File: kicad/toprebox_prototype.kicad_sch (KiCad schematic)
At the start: 1 part, among them U1 YAAJ_BlackPill_Part_Like

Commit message: completed matrix
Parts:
- U1: footprint (none) -> footprints:YAAJ_BlackPill_1
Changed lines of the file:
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@@
 			)
 		)
-		(property "Footprint" ""
+		(property "Footprint" "footprints:YAAJ_BlackPill_1"
 			(at 106.68 43.18 0)
 			(effects

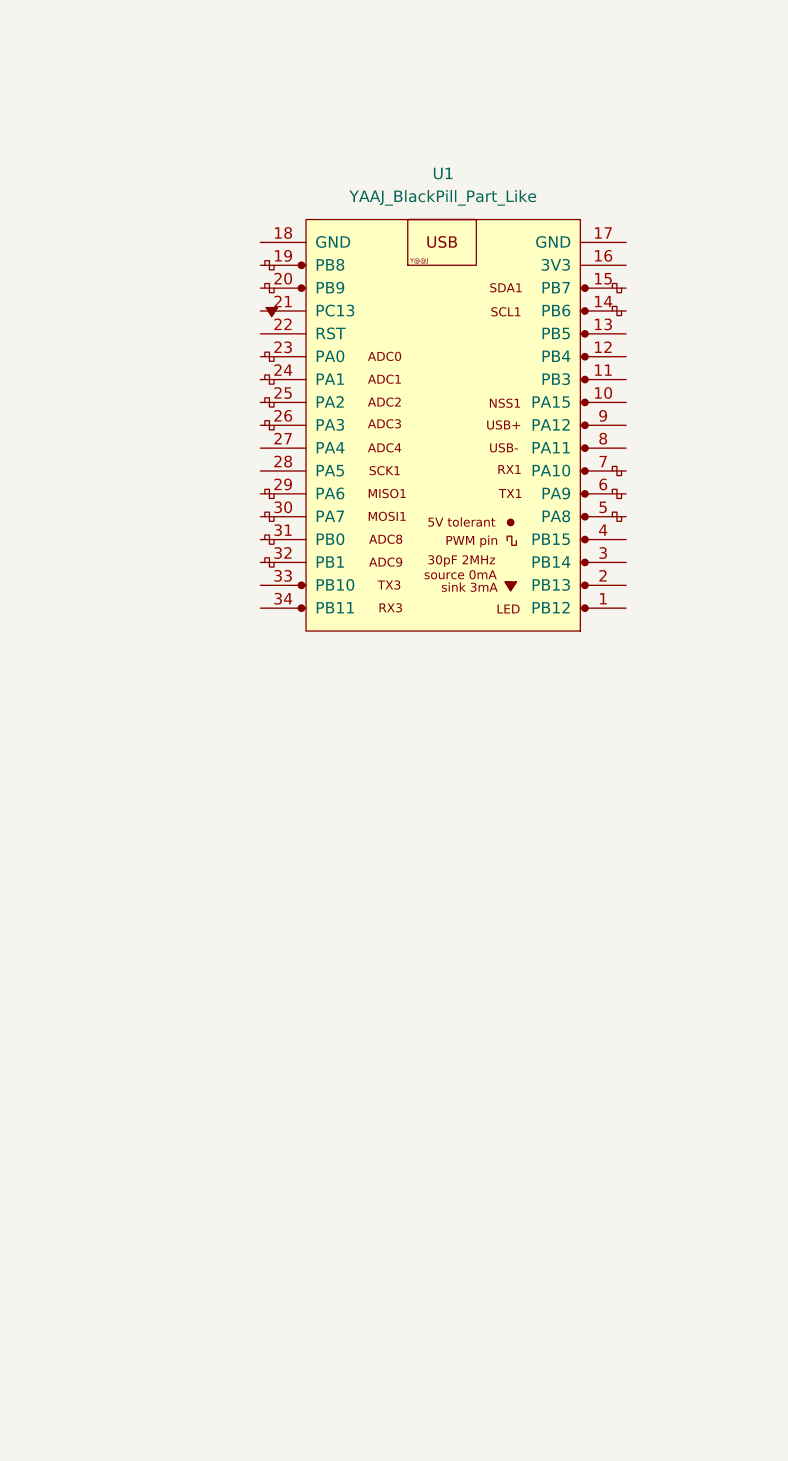
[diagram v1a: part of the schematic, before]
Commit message: replaced half of the matrix
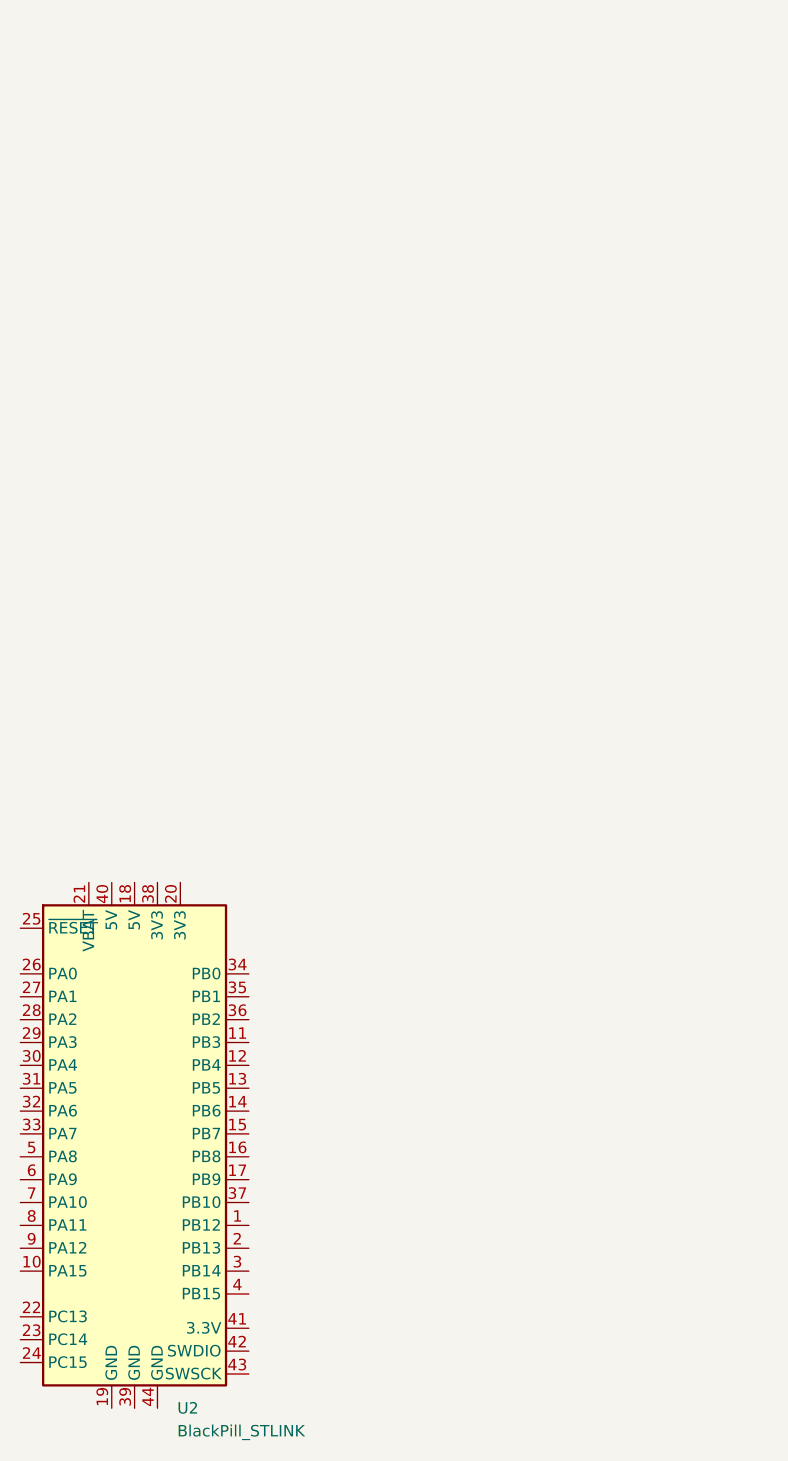
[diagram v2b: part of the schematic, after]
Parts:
- removed U1: YAAJ_BlackPill_Part_Like, footprints:YAAJ_BlackPill_1, symbol YAAJ_BlackPill_Part_Like:YAAJ_BlackPill_Part_Like
- added U2: BlackPill_STLINK, footprints:WeAct_BlackPill_without_SWD_First_Row, symbol blackpill_stlink:BlackPill_STLINK
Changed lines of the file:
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@@
 	(paper "A4")
 	(symbol
-		(lib_id "YAAJ_BlackPill_Part_Like:YAAJ_BlackPill_Part_Like")
-		(at 123.19 73.66 180)
+		(lib_id "blackpill_stlink:BlackPill_STLINK")
+		(at 88.9 154.94 0)
 		(unit 1)
 		(exclude_from_sim no)
@@
 		(dnp no)
 		(fields_autoplaced yes)
-		(property "Reference" "U1"
-			(at 123.19 45.72 0)
+		(property "Reference" "U2"
+			(at 93.6341 182.88 0)
 			(effects
 				(font
 					(size 1.27 1.27)
 				)
+				(justify left)
 			)
 		)
-		(property "Value" "YAAJ_BlackPill_Part_Like"
-			(at 123.19 48.26 0)
+		(property "Value" "BlackPill_STLINK"
+			(at 93.6341 185.42 0)
 			(effects
 				(font
 					(size 1.27 1.27)
 				)
+				(justify left)
 			)
 		)
-		(property "Footprint" "footprints:YAAJ_BlackPill_1"
-			(at 106.68 43.18 0)
+		(property "Footprint" "footprints:WeAct_BlackPill_without_SWD_First_Row"
+			(at 132.08 156.21 0)
 			(effects
 				(font
@@
 		)
 		(property "Datasheet" ""
-			(at 106.68 43.18 0)
+			(at 132.08 156.21 0)
 			(effects
 				(font
@@
 			)
 		)
-		(property "Description" ""
-			(at 123.19 73.66 0)
+		(property "Description" "STM32F4-based \"Black Pill\" micro-controller development board"
+			(at 88.9 154.94 0)
 			(effects
 				(font
@@
 			)
 		)
+		(pin "38"
+		)
+		(pin "30"
+		)
+		(pin "16"
+		)
+		(pin "4"
+		)
+		(pin "34"
+		)
+		(pin "6"
+		)
+		(pin "5"
+		)
+		(pin "7"
+		)
+		(pin "10"
+		)
+		(pin "22"
+		)
+		(pin "8"
+		)
+		(pin "26"
+		)
+		(pin "31"
+		)
+		(pin "21"
+		)
+		(pin "43"
+		)
+		(pin "36"
+		)
+		(pin "18"
+		)
+		(pin "37"
+		)
+		(pin "41"
+		)
 		(pin "28"
-		)
-		(pin "19"
 		)
 		(pin "9"
 		)
-		(pin "7"
+		(pin "17"
 		)
-		(pin "6"
+		(pin "40"
 		)
-		(pin "8"
-		)
-		(pin "16"
-		)
-		(pin "10"
-		)
-		(pin "11"
-		)
-		(pin "22"
-		)
-		(pin "15"
-		)
-		(pin "21"
-		)
-		(pin "31"
-		)
-		(pin "14"
-		)
-		(pin "13"
-		)
-		(pin "12"
-		)
-		(pin "1"
+		(pin "27"
 		)
 		(pin "20"
@@
 		(pin "25"
 		)
-		(pin "18"
+		(pin "23"
+		)
+		(pin "32"
+		)
+		(pin "33"
+		)
+		(pin "44"
+		)
+		(pin "35"
+		)
+		(pin "2"
+		)
+		(pin "39"
 		)
 		(pin "24"
 		)
-		(pin "32"
-		)
-		(pin "4"
-		)
-		(pin "27"
+		(pin "42"
 		)
 		(pin "29"
 		)
-		(pin "2"
+		(pin "1"
 		)
-		(pin "33"
+		(pin "13"
 		)
-		(pin "5"
+		(pin "19"
 		)
-		(pin "23"
+		(pin "11"
 		)
-		(pin "26"
+		(pin "12"
 		)
-		(pin "30"
+		(pin "14"
 		)
-		(pin "17"
-		)
-		(pin "34"
+		(pin "15"
 		)
 		(pin "3"
@@
 			(project ""
 				(path "/8da5c518-ba63-450e-856e-258a7a1195e6"
-					(reference "U1")
+					(reference "U2")
 					(unit 1)
 				)

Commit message: stuff
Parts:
- removed U2: BlackPill_STLINK, footprints:WeAct_BlackPill_without_SWD_First_Row, symbol blackpill_stlink:BlackPill_STLINK
- added C5, C7, C8: 100n, Capacitor_SMD:C_0402_1005Metric, symbol Device:C
- added C6: 220p, Capacitor_SMD:C_0402_1005Metric, symbol Device:C
- added JP2: Ext_Res, Resistor_SMD:R_0603_1608Metric_Pad0.98x0.95mm_HandSolder, symbol Jumper:Jumper_2_Open
- added R19, R20, R21, R22, R23, R24, R25, R26, R27, R29, R30, R31, R32, R33, R34, R35, R36: 100k, Resistor_SMD:R_0402_1005Metric, symbol Device:R
- added R28: 1k, Resistor_SMD:R_0402_1005Metric, symbol Device:R
- added U2, U7: 74HC4051, footprints:TSSOP16, symbol 74xx:74HC4051
- added U5: Helios, footprints:RP2040_Pro_Micro, symbol PCM_marbastlib-promicroish:Helios
- added U6: OPA350, Package_SO:SOIC-8_3.9x4.9mm_P1.27mm, symbol burrbrown:OPA350
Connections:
- new net: R31.1, U7.15 (A2)
- new net: JP2.2 (B), R19.2, R28.1, U6.2 (IN-)
- new net: R30.1, U7.14 (A1)
- new net: R26.1, U2.2 (A6)
- new net: R27.1, U2.4 (A7)
- new net: R32.1, U7.12 (A3)
- new net: R29.1, U7.13 (A0)
- new net: R36.1, U7.4 (A7)
- new net: R34.1, U7.5 (A5)
- new net +3V3: C5.2, C7.2, C8.2, U2.16 (VCC), U5.16 (3V3), U6.7 (V+), U7.16 (VCC)
- new net ADC: JP2.1 (A), R19.1, U5.24 (P21), U6.6 (OUT)
- new net AMUX_SEL_0: U2.11 (S0), U5.28 (P15), U7.11 (S0)
- new net AMUX_SEL_1: U2.10 (S1), U5.27 (P14), U7.10 (S1)
- new net AMUX_SEL_2: U2.9 (S2), U5.26 (P13), U7.9 (S2)
- new net APLEX_EN_PIN_0: U2.6 (~{E}), U5.29 (P16)
- new net APLEX_EN_PIN_1: U5.25 (P12), U7.6 (~{E})
- new net APLEX_OUT_PIN_0: C6.1, U2.3 (A), U6.3 (IN+), U7.3 (A)
- new net C0: R20.1, U2.13 (A0)
- new net C1: R21.1, U2.14 (A1)
- new net C2: R22.1, U2.15 (A2)
- new net C3: R23.1, U2.12 (A3)
- new net C4: R24.1, U2.1 (A4)
- new net C5: R25.1, U2.5 (A5)
- new net C6: R33.1, U7.1 (A4)
- new net C7: R35.1, U7.2 (A6)
- new net GND: C5.1, C6.2, C7.1, C8.1, R20.2, R21.2, R22.2, R23.2, R24.2, R25.2, R26.2, R27.2, R28.2, R29.2, R30.2, R31.2, R32.2, R33.2, R34.2, R35.2, R36.2, U2.7 (VEE), U2.8 (GND), U5.14 (GND), U5.3 (GND), U5.4 (GND), U6.4 (V-), U7.7 (VEE), U7.8 (GND)
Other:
- removed sheet analog
- added sheet mountingholes (mountingholes.kicad_sch)
